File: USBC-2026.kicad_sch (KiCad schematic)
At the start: 28 parts, among them IC1 TPS25752ASRSMR, J1 USB_C_Receptacle, Q1 NMOS_Substrate, Q2 NMOS_Substrate, U1 TPS55288RPMR

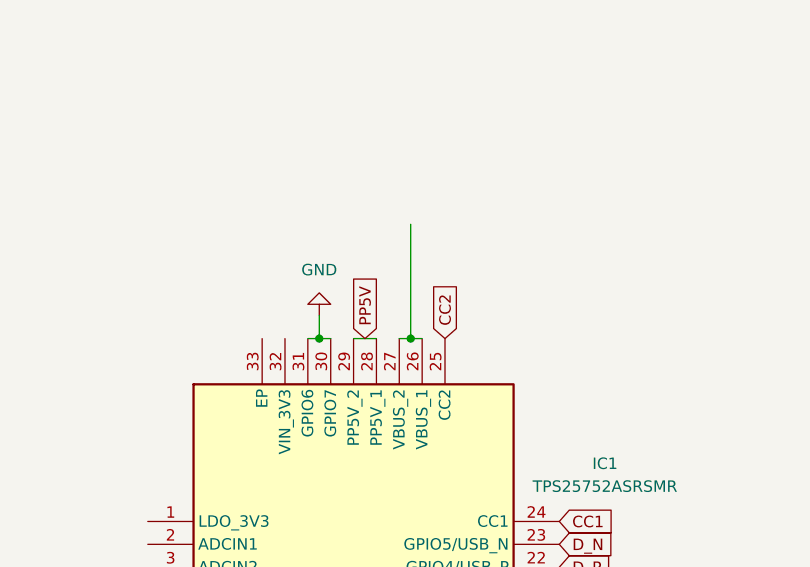
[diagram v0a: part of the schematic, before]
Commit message: Connected Vbus and PP5V to CD PD IC.
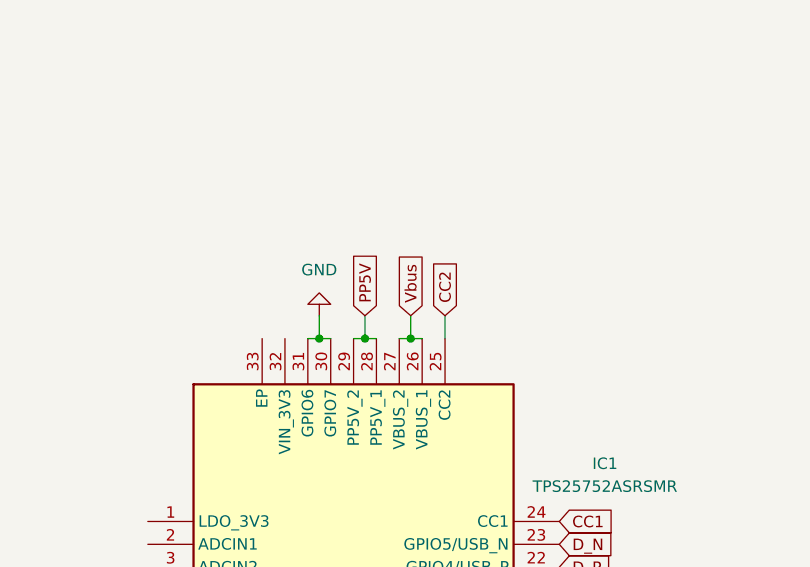
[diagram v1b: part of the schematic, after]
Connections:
- net Vbus: now also IC1.26 (VBUS_1), IC1.27 (VBUS_2)
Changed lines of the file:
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@@
+	)
+	(junction
+		(at 168.91 76.2)
+		(diameter 0)
+		(color 0 0 0 0)
 	)
 	(junction
@@
 	(wire
 		(pts
+			(xy 168.91 76.2) (xy 170.18 76.2)
+		)
+		(stroke
+			(width 0)
+			(type default)
+		)
+	)
+	(wire
+		(pts
 			(xy 24.13 184.15) (xy 26.67 184.15)
 		)
@@
 	(wire
 		(pts
-			(xy 167.64 76.2) (xy 170.18 76.2)
+			(xy 167.64 76.2) (xy 168.91 76.2)
 		)
 		(stroke
@@
 	(wire
 		(pts
+			(xy 168.91 73.66) (xy 168.91 76.2)
+		)
+		(stroke
+			(width 0)
+			(type default)
+		)
+	)
+	(wire
+		(pts
 			(xy 46.99 179.07) (xy 48.26 179.07)
 		)
@@
 	(wire
 		(pts
-			(xy 173.99 63.5) (xy 173.99 76.2)
+			(xy 173.99 73.66) (xy 173.99 76.2)
 		)
 		(stroke
@@
 	(wire
 		(pts
+			(xy 177.8 73.66) (xy 177.8 76.2)
+		)
+		(stroke
+			(width 0)
+			(type default)
+		)
+	)
+	(wire
+		(pts
 			(xy 24.13 176.53) (xy 30.48 176.53)
 		)
@@
 	(global_label "Vbus"
 		(shape input)
+		(at 173.99 73.66 90)
+		(fields_autoplaced yes)
+		(effects
+			(font
+				(size 1.27 1.27)
+			)
+			(justify left)
+		)
+		(property "Intersheetrefs" "${INTERSHEET_REFS}"
+			(at 173.99 66.2601 90)
+			(hide yes)
+			(show_name no)
+			(do_not_autoplace no)
+			(effects
+				(font
+					(size 1.27 1.27)
+				)
+				(justify left)
+			)
+		)
+	)
+	(global_label "Vbus"
+		(shape input)
 		(at 24.13 184.15 180)
 		(fields_autoplaced yes)
@@
 	(global_label "CC2"
 		(shape input)
-		(at 177.8 76.2 90)
+		(at 177.8 73.66 90)
 		(fields_autoplaced yes)
 		(effects
@@
 		)
 		(property "Intersheetrefs" "${INTERSHEET_REFS}"
-			(at 177.8 69.4653 90)
+			(at 177.8 66.9253 90)
 			(hide yes)
 			(show_name no)
@@
 	(global_label "PP5V"
 		(shape input)
-		(at 168.91 76.2 90)
+		(at 168.91 73.66 90)
 		(fields_autoplaced yes)
 		(effects
@@
 		)
 		(property "Intersheetrefs" "${INTERSHEET_REFS}"
-			(at 168.91 68.3767 90)
-			(hide yes)
-			(show_name no)
+			(at 168.91 65.8367 90)
+			(hide yes)
+			(show_name no)

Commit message: Removed 5V converter.
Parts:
- removed C10: 200n, symbol Device:C
- removed C11: 45p, symbol Device:C
- removed C12, C13: 22u, symbol Device:C
- removed C9: 10u, symbol Device:C
- removed L1: 3.3u, symbol Device:L
- removed MOSFET1: AP62300WU-7, TSOT26_DIO, symbol symbol_library:AP62300WU-7
- removed R4: 52.3k, symbol Device:R_US
- removed R5: 10k, symbol Device:R_US
- removed R6: 14M, symbol Device:R_US
- removed R7: 10M, symbol Device:R_US
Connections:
- net PP5V renamed +5V
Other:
- note removed: "****5V,3A Buck****"
- note removed: "/\ This one is optional"

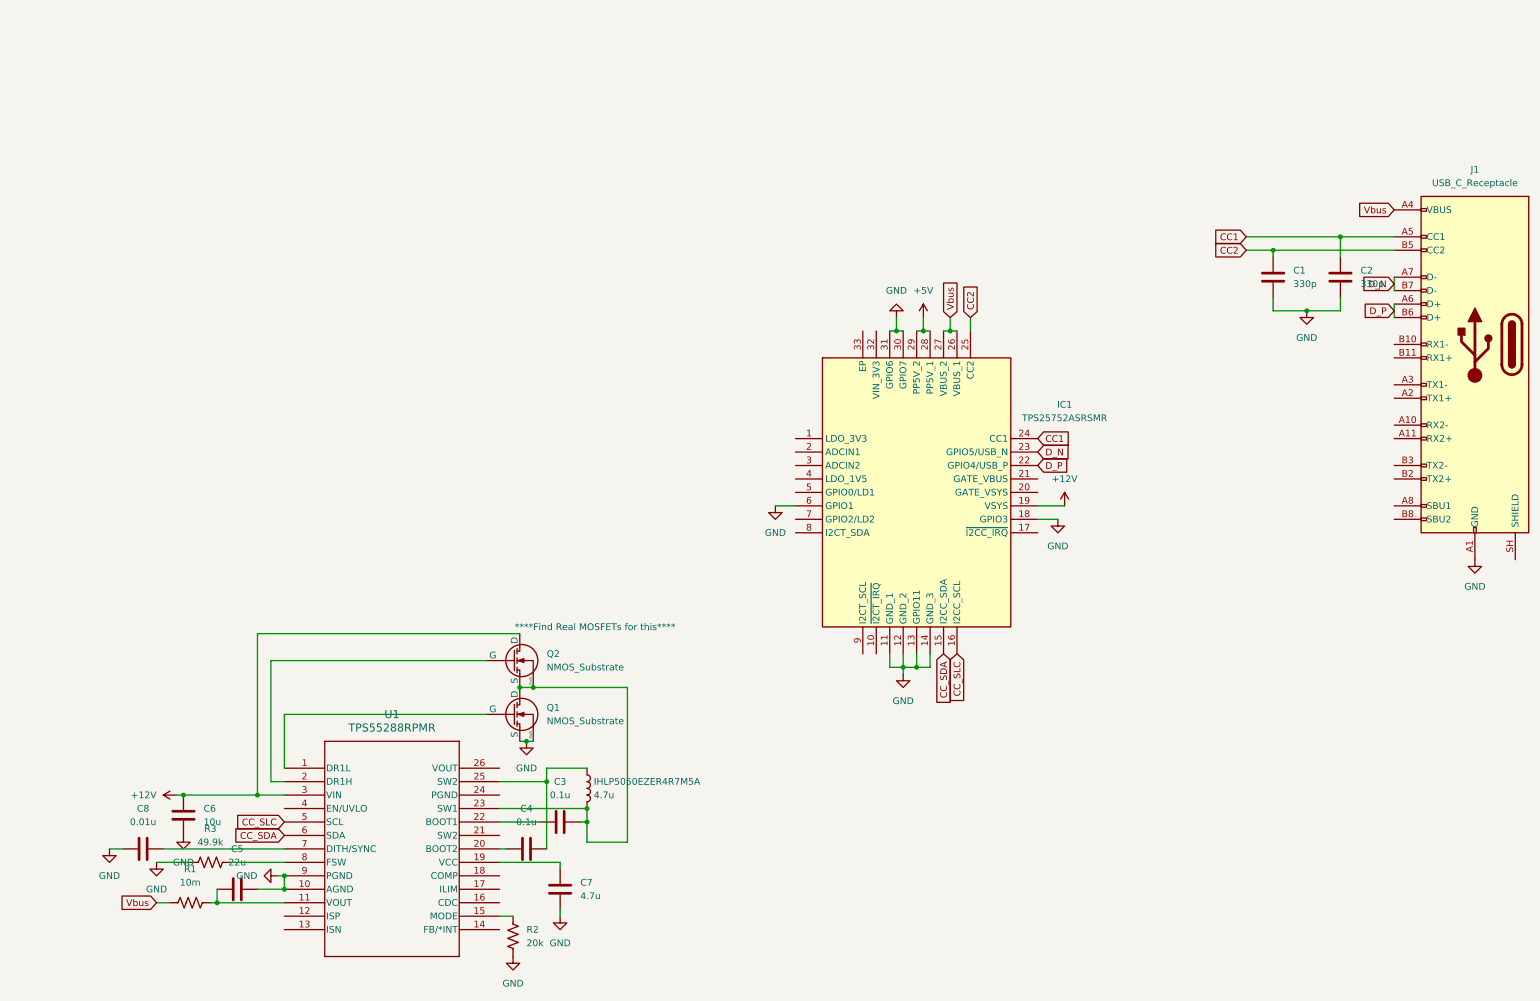
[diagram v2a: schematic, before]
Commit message: Connected PD controller 3v3 and 1v5.
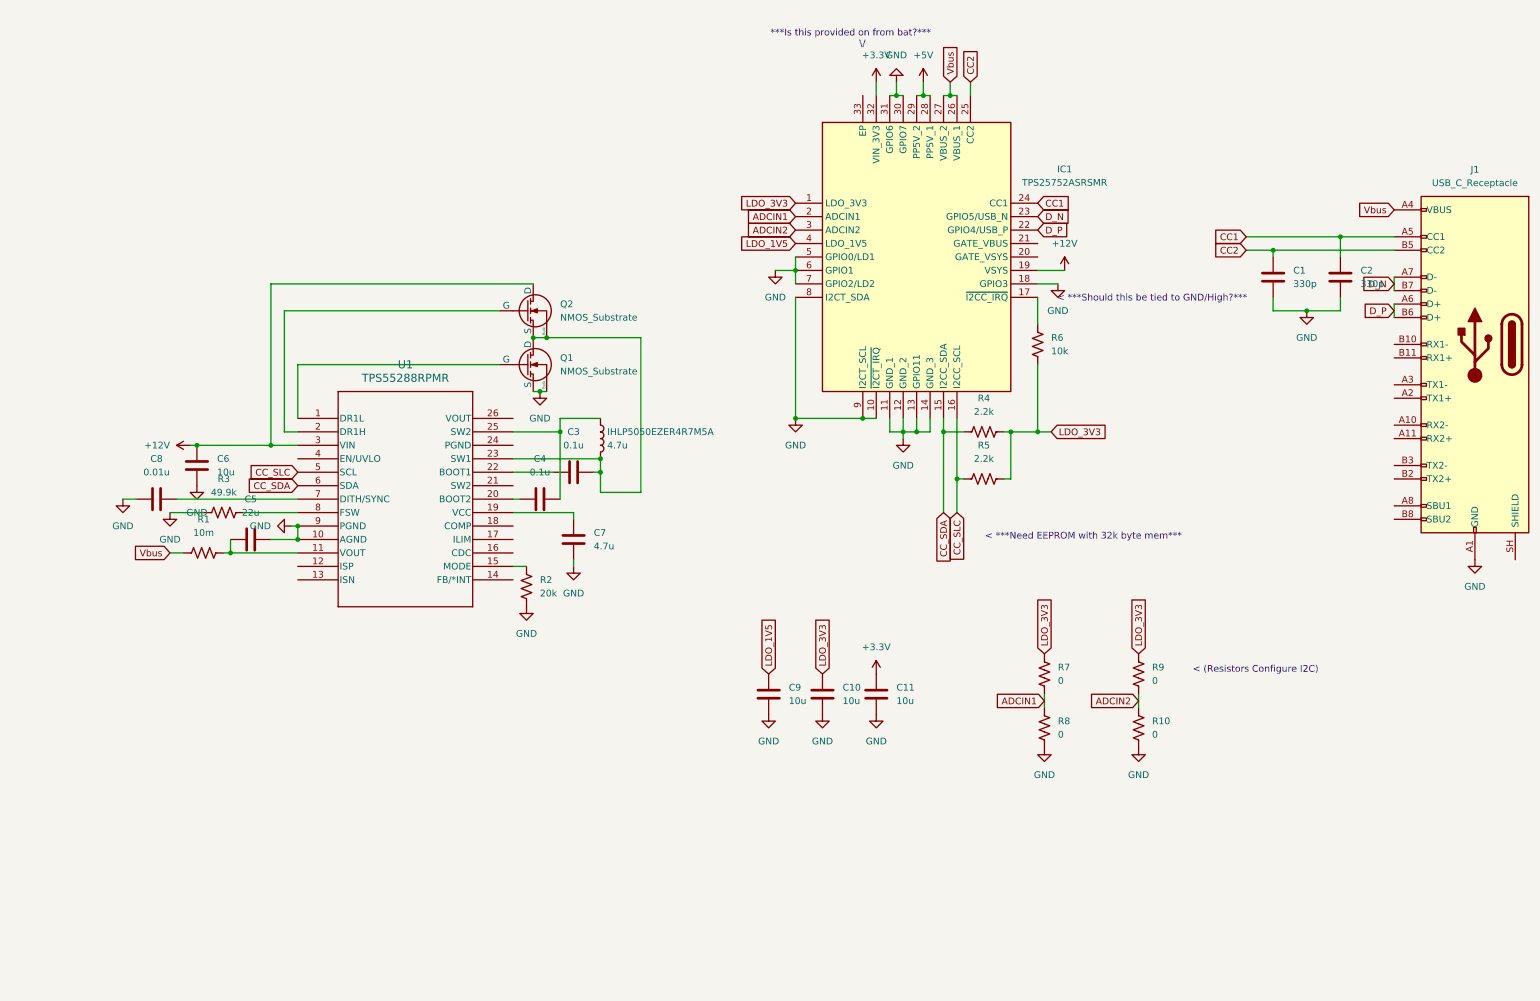
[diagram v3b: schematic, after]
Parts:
- added C10, C11, C9: 10u, symbol Device:C
- added R10, R7, R8, R9: 0, symbol Device:R_US
- added R4, R5: 2.2k, symbol Device:R_US
- added R6: 10k, symbol Device:R_US
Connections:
- net CC_SDA: now also R4.1
- net CC_SLC: now also R5.1
- net GND: now also IC1.10 (~{I2CT_IRQ}), IC1.5 (GPIO0/LD1), IC1.7 (GPIO2/LD2), IC1.8 (I2CT_SDA), IC1.9 (I2CT_SCL), C10.1, C11.2, C9.1, R10.2, R8.2
- net LDO_3V3: now reaches IC1.1 (LDO_3V3)
- net LDO_3V3: now also C10.2, R4.2, R5.2, R6.1, R7.1, R9.1
- net at IC1.17 (~{I2CC_IRQ}): now also R6.2
- net ADCIN1: now reaches IC1.2 (ADCIN1)
- net ADCIN1: now also R7.2, R8.1
- net ADCIN2: now reaches IC1.3 (ADCIN2)
- net ADCIN2: now also R10.1, R9.2
- net +3.3V: now reaches IC1.32 (VIN_3V3)
- net +3.3V: now also C11.1
- net LDO_1V5: now reaches IC1.4 (LDO_1V5)
- net LDO_1V5: now also C9.2
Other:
- note added: "***Is this provided on from bat?*** \/"
- note added: "< (Resistors Configure I2C)"
- note added: "< ***Need EEPROM with 32k byte mem***"
- note added: "< ***Should this be tied to GND/High?***"
- note removed: "****Find Real MOSFETs for this****"
- moved on the sheet: C3, C4, C5, C6, C7, C8, IC1, IHLP5050EZER4R7M5A, Q1, Q2, R1, R2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

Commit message: Imported PD controller EEPROM.
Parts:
- added U2: AT24C512C-SHM-B, 8X_MCH, symbol symbol_library:AT24C512C-SHM-B
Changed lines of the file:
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@@
+	)
+	(symbol
+		(lib_id "symbol_library:AT24C512C-SHM-B")
+		(at 60.96 45.72 0)
+		(unit 1)
+		(body_style 1)
+		(exclude_from_sim no)
+		(in_bom yes)
+		(on_board yes)
+		(in_pos_files yes)
+		(dnp no)
+		(fields_autoplaced yes)
+		(property "Reference" "U2"
+			(at 88.9 35.56 0)
+			(show_name no)
+			(do_not_autoplace no)
+			(effects
+				(font
+					(size 1.524 1.524)
+				)
+			)
+		)
+		(property "Value" "AT24C512C-SHM-B"
+			(at 88.9 38.1 0)
+			(show_name no)
+			(do_not_autoplace no)
+			(effects
+				(font
+					(size 1.524 1.524)
+				)
+			)
+		)
+		(property "Footprint" "8X_MCH"
+			(at 60.96 45.72 0)
+			(hide yes)
+			(show_name no)
+			(do_not_autoplace no)
+			(effects
+				(font
+					(size 1.27 1.27)
+					(italic yes)
+				)
+			)
+		)
+		(property "Datasheet" "AT24C512C-SHM-B"
+			(at 60.96 45.72 0)
+			(hide yes)
+			(show_name no)
+			(do_not_autoplace no)
+			(effects
+				(font
+					(size 1.27 1.27)
+					(italic yes)
+				)
+			)
+		)
+		(property "Description" ""
+			(at 60.96 45.72 0)
+			(hide yes)
+			(show_name no)
+			(do_not_autoplace no)
+			(effects
+				(font
+					(size 1.27 1.27)
+				)
+			)
+		)
+		(pin "1"
+		)
+		(pin "8"
+		)
+		(pin "7"
+		)
+		(pin "6"
+		)
+		(pin "5"
+		)
+		(pin "4"
+		)
+		(pin "3"
+		)
+		(pin "2"
+		)
+		(instances
+			(project "USBC-2026"
+				(path "/0c056c42-d02c-4bee-adc4-fcbb18375f33"
+					(reference "U2")
+					(unit 1)
+				)
+			)
+		)
 	)
 	(symbol

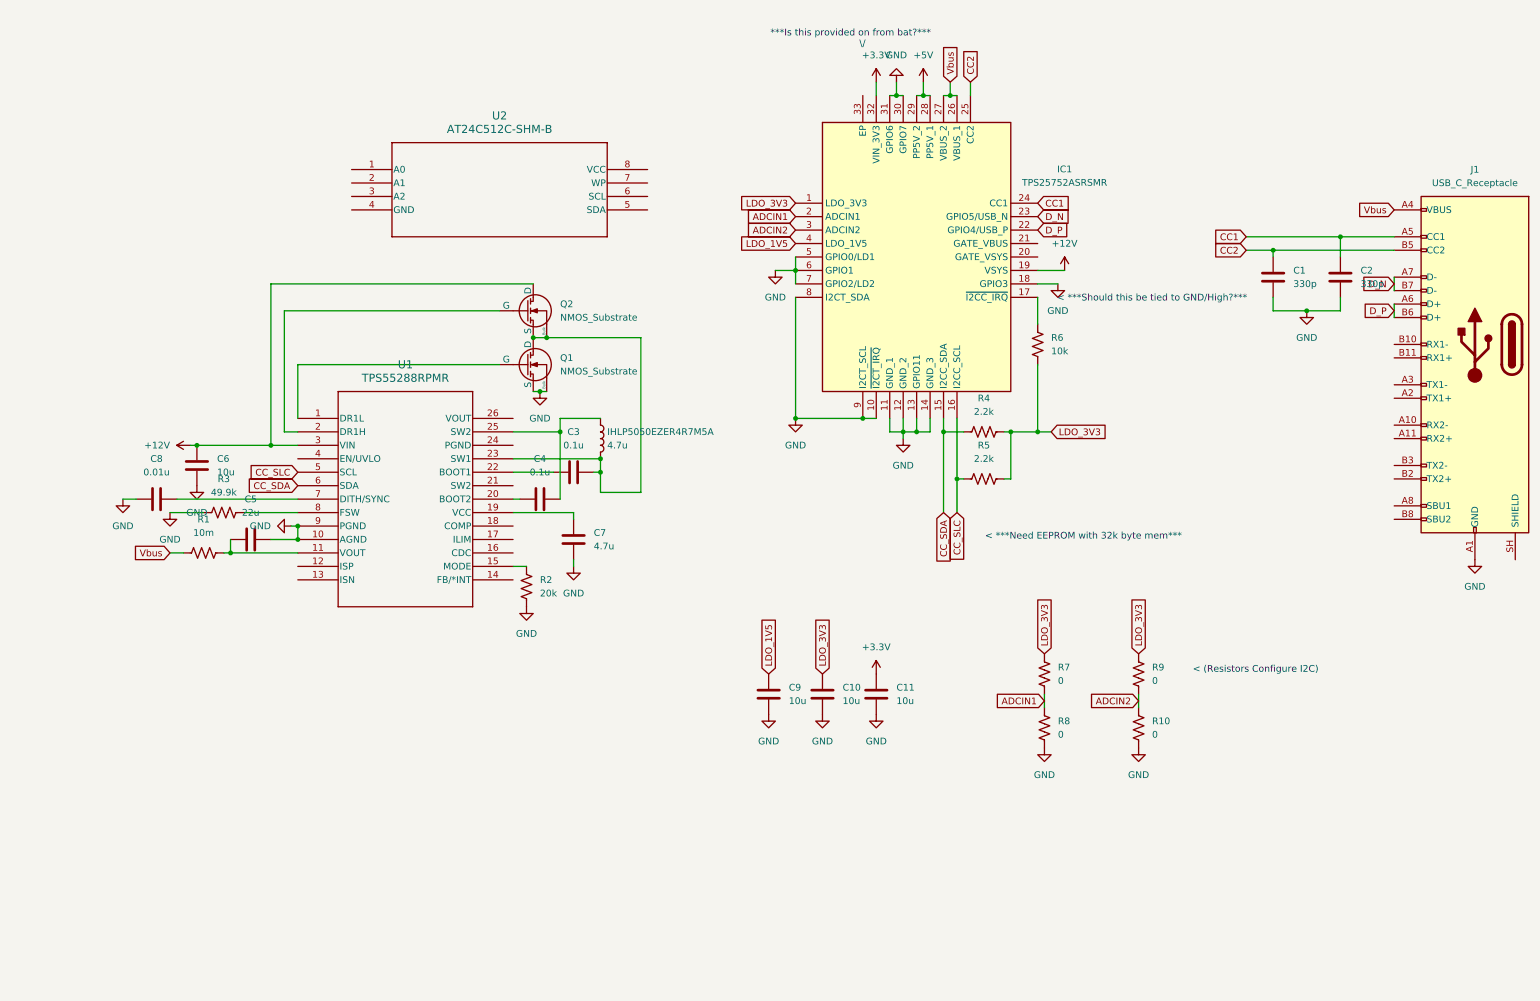
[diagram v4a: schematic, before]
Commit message: Connected pins of EEPROM.
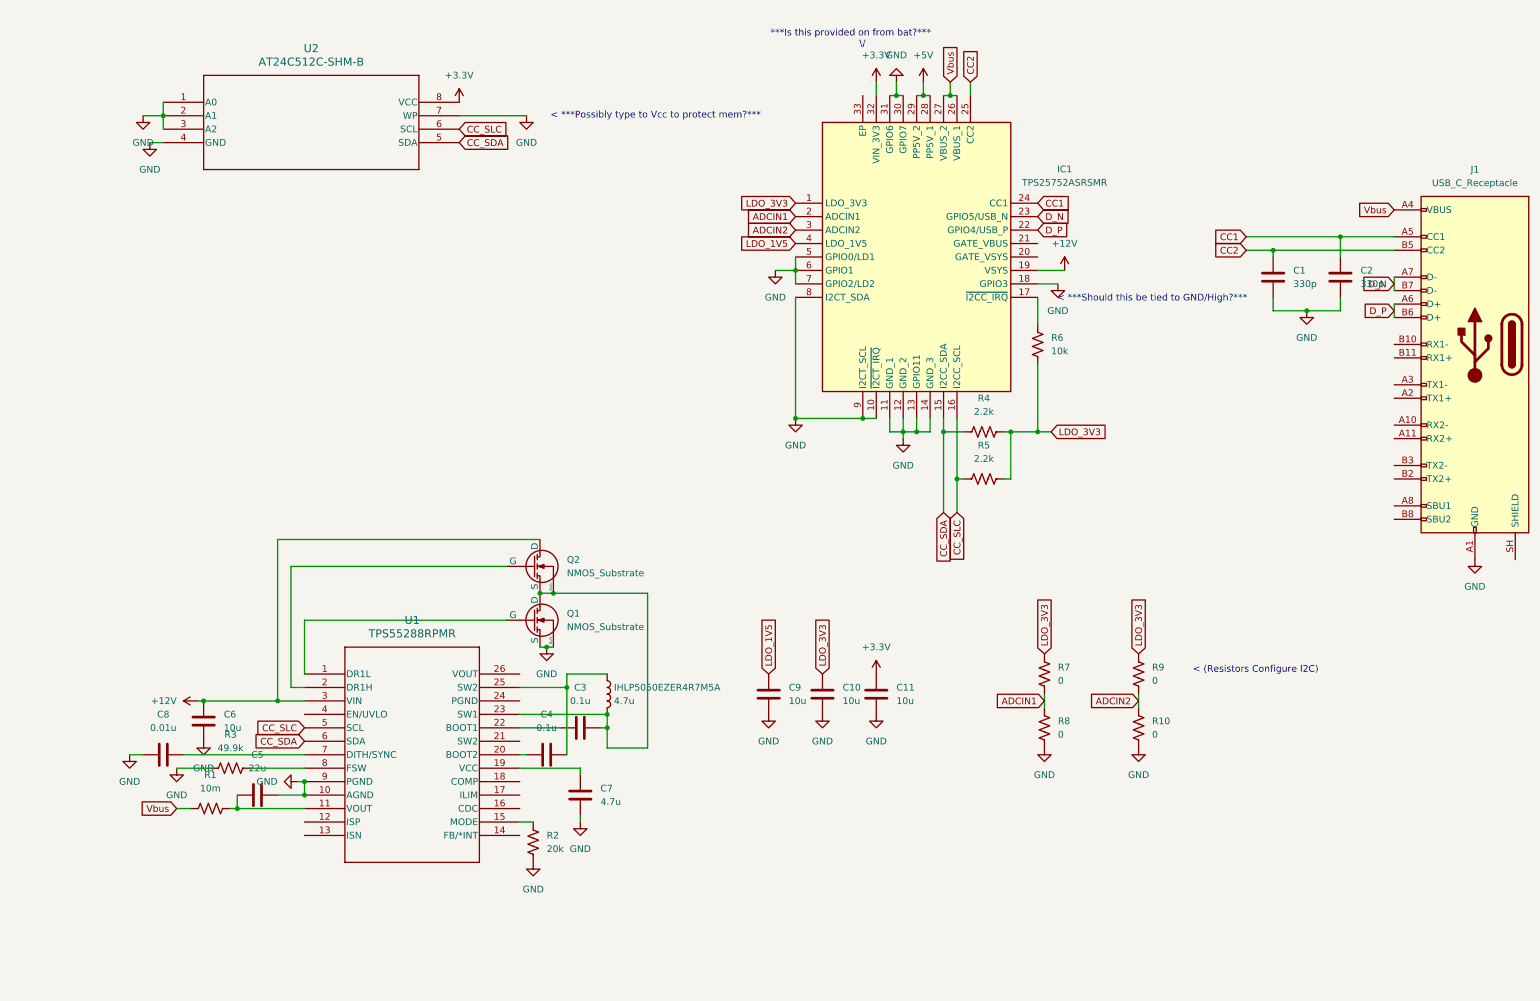
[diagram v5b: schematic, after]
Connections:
- net +3.3V: now also U2.8 (VCC)
- net CC_SDA: now also U2.5 (SDA)
- net CC_SLC: now also U2.6 (SCL)
- net GND: now also U2.1 (A0), U2.2 (A1), U2.3 (A2), U2.4 (GND), U2.7 (WP)
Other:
- note added: "< ***Possibly type to Vcc to protect mem?***"
- note removed: "< ***Need EEPROM with 32k byte mem***"
- moved on the sheet: C3, C4, C5, C6, C7, C8, IHLP5050EZER4R7M5A, Q1, Q2, R1, R2, R3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
